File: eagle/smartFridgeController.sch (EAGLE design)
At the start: 12 parts

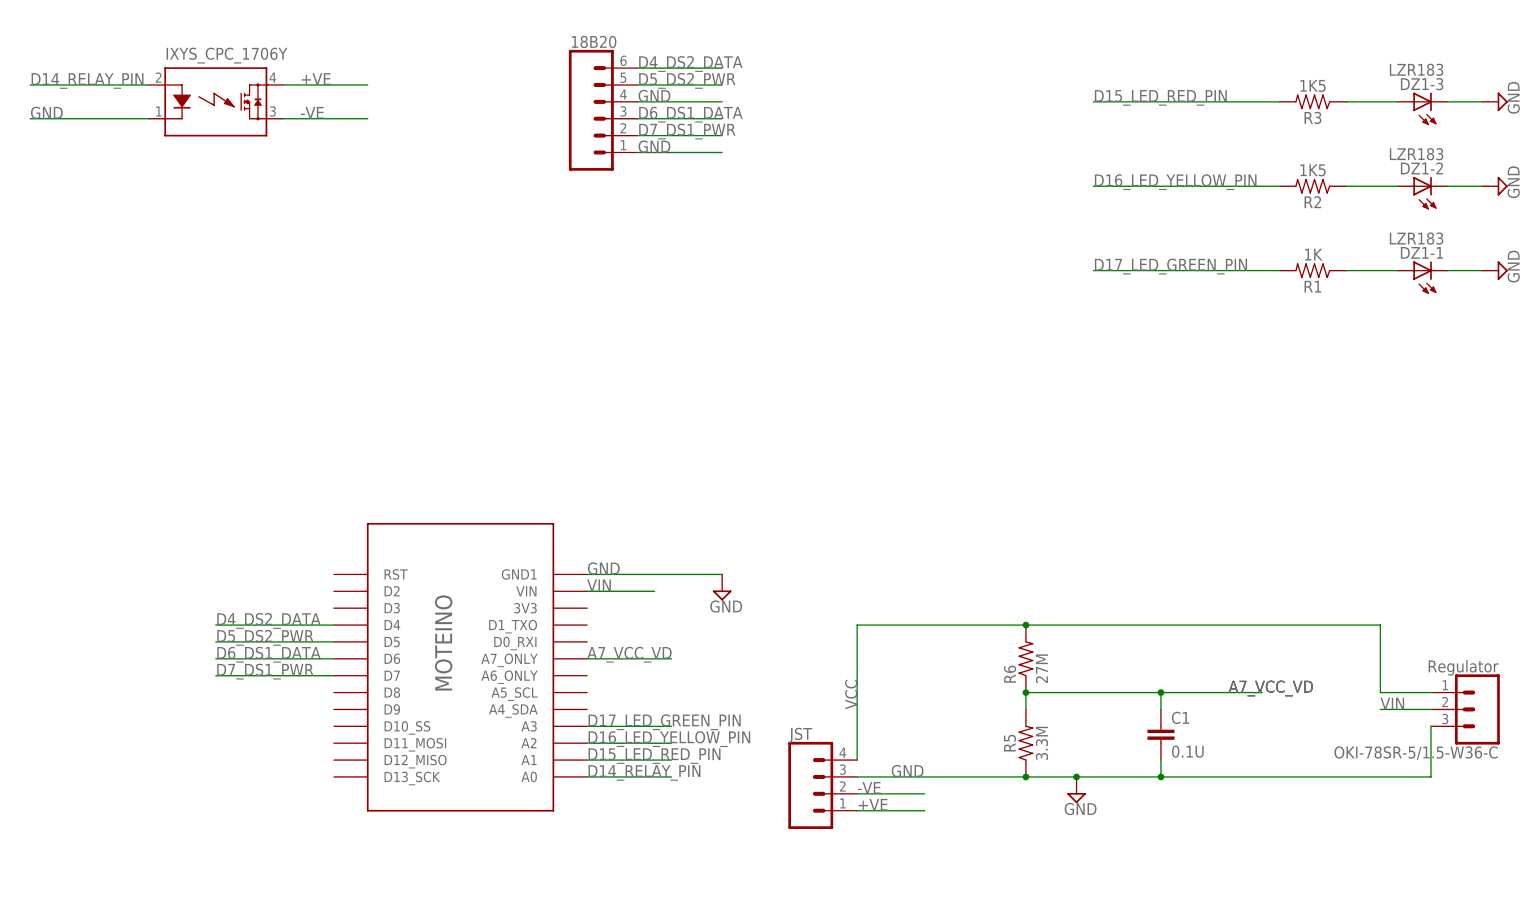
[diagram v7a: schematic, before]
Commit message: Added gititgnore
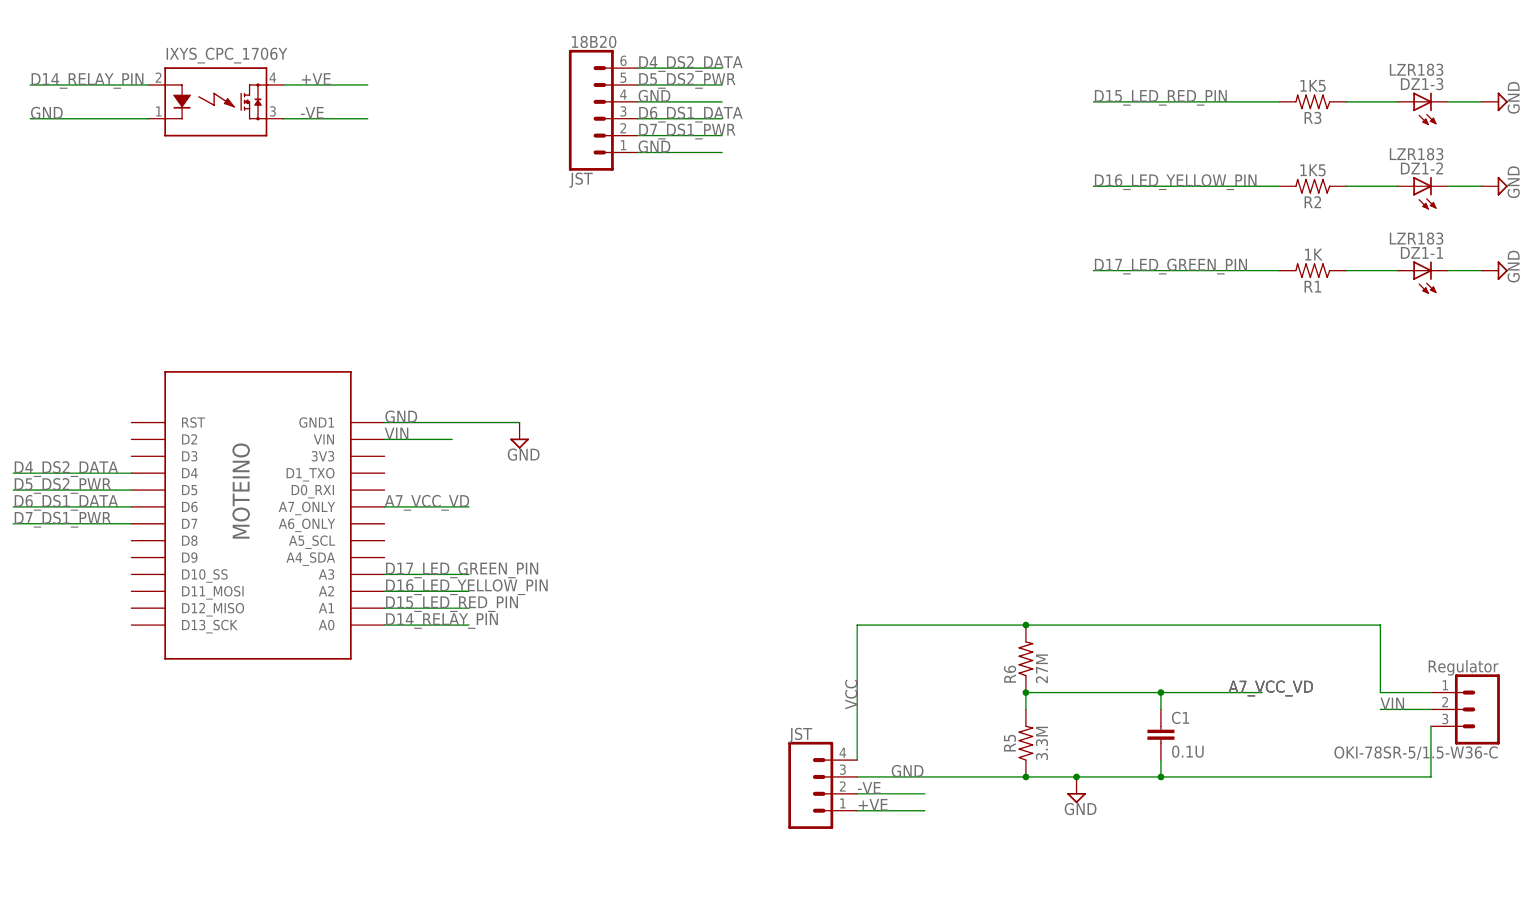
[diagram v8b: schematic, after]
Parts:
- 18B20: value (none) -> JST
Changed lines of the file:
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@@
 <part name="SUPPLY3" library="supply2" deviceset="GND" device=""/>
 <part name="OKI-78SR-5/1.5-W36-C" library="SparkFun-Connectors" deviceset="CONN_03" device="" value="Regulator"/>
-<part name="18B20" library="SparkFun-Connectors" deviceset="CONN_06" device="SILK_FEMALE_PTH"/>
+<part name="18B20" library="SparkFun-Connectors" deviceset="CONN_06" device="SILK_FEMALE_PTH" value="JST"/>
 <part name="DZ1" library="led" library_urn="urn:adsk.eagle:library:259" deviceset="LZR183" device="" package3d_urn="urn:adsk.eagle:package:15788/1"/>
 <part name="R1" library="SparkFun-Resistors" deviceset="1KOHM" device="-HORIZ-1/4W-1%" value="1K"/>
@@
 <instance part="JST" gate="G$1" x="139.7" y="43.18"/>
 <instance part="R6" gate="G$1" x="170.18" y="63.5" rot="R90"/>
-<instance part="SUPPLY3" gate="GND" x="124.46" y="73.66"/>
+<instance part="SUPPLY3" gate="GND" x="93.98" y="96.52"/>
 <instance part="OKI-78SR-5/1.5-W36-C" gate="J$1" x="238.76" y="55.88" rot="R180"/>
 <instance part="18B20" gate="G$1" x="106.68" y="144.78"/>
@@
 <instance part="SUPPLY2" gate="GND" x="241.3" y="134.62" rot="R90"/>
 <instance part="SUPPLY4" gate="GND" x="241.3" y="147.32" rot="R90"/>
-<instance part="U$2" gate="G$1" x="81.28" y="58.42"/>
+<instance part="U$2" gate="G$1" x="50.8" y="81.28"/>
 <instance part="IXYS_CPC_1706Y" gate="G$1" x="48.26" y="147.32" smashed="yes">
 <attribute name="NAME" x="40.64" y="153.67" size="1.778" layer="95" font="vector"/>
@@
 </segment>
 <segment>
-<wire x1="124.46" y1="76.2" x2="104.14" y2="76.2" width="0.1524" layer="91"/>
-<label x="104.14" y="76.2" size="1.778" layer="95"/>
+<wire x1="93.98" y1="99.06" x2="73.66" y2="99.06" width="0.1524" layer="91"/>
+<label x="73.66" y="99.06" size="1.778" layer="95"/>
 <pinref part="U$2" gate="G$1" pin="GND1"/>
+<pinref part="SUPPLY3" gate="GND" pin="GND"/>
 </segment>
 <segment>
@@
 <net name="VIN" class="1">
 <segment>
-<wire x1="104.14" y1="73.66" x2="114.3" y2="73.66" width="0.1524" layer="91"/>
-<label x="104.14" y="73.66" size="1.778" layer="95"/>
+<wire x1="73.66" y1="96.52" x2="83.82" y2="96.52" width="0.1524" layer="91"/>
+<label x="73.66" y="96.52" size="1.778" layer="95"/>
 <pinref part="U$2" gate="G$1" pin="VIN"/>
 </segment>
@@
 <net name="D7_DS1_PWR" class="0">
 <segment>
-<wire x1="66.04" y1="60.96" x2="48.26" y2="60.96" width="0.1524" layer="91"/>
-<label x="48.26" y="60.96" size="1.778" layer="95"/>
+<wire x1="35.56" y1="83.82" x2="17.78" y2="83.82" width="0.1524" layer="91"/>
+<label x="17.78" y="83.82" size="1.778" layer="95"/>
 <pinref part="U$2" gate="G$1" pin="D7"/>
 </segment>
@@
 <net name="D6_DS1_DATA" class="0">
 <segment>
-<wire x1="66.04" y1="63.5" x2="48.26" y2="63.5" width="0.1524" layer="91"/>
-<label x="48.26" y="63.5" size="1.778" layer="95"/>
+<wire x1="35.56" y1="86.36" x2="17.78" y2="86.36" width="0.1524" layer="91"/>
+<label x="17.78" y="86.36" size="1.778" layer="95"/>
 <pinref part="U$2" gate="G$1" pin="D6"/>
 </segment>
@@
 <net name="D4_DS2_DATA" class="0">
 <segment>
-<wire x1="66.04" y1="68.58" x2="48.26" y2="68.58" width="0.1524" layer="91"/>
-<label x="48.26" y="68.58" size="1.778" layer="95"/>
+<wire x1="35.56" y1="91.44" x2="17.78" y2="91.44" width="0.1524" layer="91"/>
+<label x="17.78" y="91.44" size="1.778" layer="95"/>
 <pinref part="U$2" gate="G$1" pin="D4"/>
 </segment>
@@
 <net name="D15_LED_RED_PIN" class="0">
 <segment>
-<wire x1="104.14" y1="48.26" x2="116.84" y2="48.26" width="0.1524" layer="91"/>
-<label x="104.14" y="48.26" size="1.778" layer="95"/>
+<wire x1="73.66" y1="71.12" x2="86.36" y2="71.12" width="0.1524" layer="91"/>
+<label x="73.66" y="71.12" size="1.778" layer="95"/>
 <pinref part="U$2" gate="G$1" pin="A1"/>
 </segment>
@@
 <net name="D5_DS2_PWR" class="0">
 <segment>
-<wire x1="66.04" y1="66.04" x2="48.26" y2="66.04" width="0.1524" layer="91"/>
-<label x="48.26" y="66.04" size="1.778" layer="95"/>
+<wire x1="35.56" y1="88.9" x2="17.78" y2="88.9" width="0.1524" layer="91"/>
+<label x="17.78" y="88.9" size="1.778" layer="95"/>
 <pinref part="U$2" gate="G$1" pin="D5"/>
 </segment>
@@
 <net name="A7_VCC_VD" class="0">
 <segment>
-<wire x1="104.14" y1="63.5" x2="116.84" y2="63.5" width="0.1524" layer="91"/>
-<label x="104.14" y="63.5" size="1.778" layer="95"/>
+<wire x1="73.66" y1="86.36" x2="86.36" y2="86.36" width="0.1524" layer="91"/>
+<label x="73.66" y="86.36" size="1.778" layer="95"/>
 <pinref part="U$2" gate="G$1" pin="A7_ONLY"/>
 </segment>
@@
 <net name="D14_RELAY_PIN" class="0">
 <segment>
-<wire x1="104.14" y1="45.72" x2="116.84" y2="45.72" width="0.1524" layer="91"/>
-<label x="104.14" y="45.72" size="1.778" layer="95"/>
+<wire x1="73.66" y1="68.58" x2="86.36" y2="68.58" width="0.1524" layer="91"/>
+<label x="73.66" y="68.58" size="1.778" layer="95"/>
 <pinref part="U$2" gate="G$1" pin="A0"/>
 </segment>
@@
 <net name="D16_LED_YELLOW_PIN" class="0">
 <segment>
-<wire x1="104.14" y1="50.8" x2="116.84" y2="50.8" width="0.1524" layer="91"/>
-<label x="104.14" y="50.8" size="1.778" layer="95"/>
+<wire x1="73.66" y1="73.66" x2="86.36" y2="73.66" width="0.1524" layer="91"/>
+<label x="73.66" y="73.66" size="1.778" layer="95"/>
 <pinref part="U$2" gate="G$1" pin="A2"/>
 </segment>
@@
 <net name="D17_LED_GREEN_PIN" class="0">
 <segment>
-<wire x1="104.14" y1="53.34" x2="116.84" y2="53.34" width="0.1524" layer="91"/>
-<label x="104.14" y="53.34" size="1.778" layer="95"/>
+<wire x1="73.66" y1="76.2" x2="86.36" y2="76.2" width="0.1524" layer="91"/>
+<label x="73.66" y="76.2" size="1.778" layer="95"/>
 <pinref part="U$2" gate="G$1" pin="A3"/>
 </segment>
